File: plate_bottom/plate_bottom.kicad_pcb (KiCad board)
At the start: 2 copper layers, 180.2 x 118.1 mm, 0 parts

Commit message: Holes
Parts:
- added HM1: CaseHole, used_footprints:Hole_Mount_M4, F.Cu at (215.4, 123.7)
- added HM10: CaseHole, used_footprints:Hole_Mount_M4, F.Cu at (190.8, 74.8)
- added HM11: CaseHole, used_footprints:Hole_Mount_M4, F.Cu at (152.7, 68.5)
- added HM12: CaseHole, used_footprints:Hole_Mount_M4, F.Cu at (220.1, 69.2)
- added HM2: CaseHole, used_footprints:Hole_Mount_M4, F.Cu at (191.3, 55.2)
- added HM3: CaseHole, used_footprints:Hole_Mount_M4, F.Cu at (240.8, 109.5)
- added HM4: CaseHole, used_footprints:Hole_Mount_M4, F.Cu at (164.4, 116.7)
- added HM5: CaseHole, used_footprints:Hole_Mount_M4, F.Cu at (95.5, 98.6)
- added HM6: CaseHole, used_footprints:Hole_Mount_M4, F.Cu at (114.6, 98.7)
- added HM7: CaseHole, used_footprints:Hole_Mount_M4, F.Cu at (114.5, 59.9)
- added HM8: CaseHole, used_footprints:Hole_Mount_M4, F.Cu at (114.5, 79.7)
- added HM9: CaseHole, used_footprints:Hole_Mount_M4, F.Cu at (152.7, 53.4)
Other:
- outline, holes or cut-outs redrawn
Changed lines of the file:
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@@
     (tracks 0)
     (zones 0)
-    (modules 0)
+    (modules 12)
     (nets 1)
   )
@@
     (uvia_drill 0.1)
   )
+  (module used_footprints:Hole_Mount_M4 (layer F.Cu)
+    (at 215.4 123.65 36)
+    (fp_text reference HM1 (at -0.01 -2.09 36) (layer F.SilkS) hide
+      (effects (font (size 1 1) (thickness 0.15)))
+    )
+    (fp_text value CaseHole (at 0.5 -3.77 36) (layer F.Fab) hide
+      (effects (font (size 1 1) (thickness 0.15)))
+    )
+    (pad "" np_thru_hole circle (at -0.117557 0.161803 36) (size 2.2 2.2) (drill 2.2) (layers *.Cu *.Mask))
+  )
+  (module used_footprints:Hole_Mount_M4 (layer F.Cu)
+    (at 164.44712 116.70512)
+    (fp_text reference HM4 (at -0.01 -2.09) (layer Dwgs.User) hide
+      (effects (font (size 1 1) (thickness 0.15)))
+    )
+    (fp_text value CaseHole (at 0.5 -3.77) (layer F.Fab) hide
+      (effects (font (size 1 1) (thickness 0.15)))
+    )
+    (pad "" np_thru_hole circle (at 0.00288 -0.70512) (size 2.2 2.2) (drill 2.2) (layers *.Cu *.Mask))
+  )
+  (module used_footprints:Hole_Mount_M4 (layer F.Cu)
+    (at 114.55 59.9)
+    (fp_text reference HM7 (at -0.01 -2.09) (layer F.SilkS) hide
+      (effects (font (size 1 1) (thickness 0.15)))
+    )
+    (fp_text value CaseHole (at 0.5 -3.77) (layer F.Fab) hide
+      (effects (font (size 1 1) (thickness 0.15)))
+    )
+    (pad "" np_thru_hole circle (at 0 0) (size 2.2 2.2) (drill 2.2) (layers *.Cu *.Mask))
+  )
+  (module used_footprints:Hole_Mount_M4 (layer F.Cu)
+    (at 152.65 53.35)
+    (fp_text reference HM9 (at -0.01 -2.09) (layer F.SilkS) hide
+      (effects (font (size 1 1) (thickness 0.15)))
+    )
+    (fp_text value CaseHole (at 0.5 -3.77) (layer F.Fab) hide
+      (effects (font (size 1 1) (thickness 0.15)))
+    )
+    (pad "" np_thru_hole circle (at -0.65 -0.5) (size 2.2 2.2) (drill 2.2) (layers *.Cu *.Mask))
+  )
+  (module used_footprints:Hole_Mount_M4 (layer F.Cu)
+    (at 190.75 74.85)
+    (fp_text reference HM10 (at -0.01 -2.09) (layer F.SilkS) hide
+      (effects (font (size 1 1) (thickness 0.15)))
+    )
+    (fp_text value CaseHole (at 0.5 -3.77) (layer F.Fab) hide
+      (effects (font (size 1 1) (thickness 0.15)))
+    )
+    (pad "" np_thru_hole circle (at 0 0) (size 2.2 2.2) (drill 2.2) (layers *.Cu *.Mask))
+  )
+  (module used_footprints:Hole_Mount_M4 (layer F.Cu)
+    (at 95.5 98.56832)
+    (fp_text reference HM5 (at -0.01 -2.09) (layer Dwgs.User) hide
+      (effects (font (size 1 1) (thickness 0.15)))
+    )
+    (fp_text value CaseHole (at 0.5 -3.77) (layer F.Fab) hide
+      (effects (font (size 1 1) (thickness 0.15)))
+    )
+    (pad "" np_thru_hole circle (at 0 0.08168) (size 2.2 2.2) (drill 2.2) (layers *.Cu *.Mask))
+  )
+  (module used_footprints:Hole_Mount_M4 (layer F.Cu)
+    (at 191.2725 55.183451 14.5)
+    (fp_text reference HM2 (at -0.01 -2.09 14.5) (layer Dwgs.User) hide
+      (effects (font (size 1 1) (thickness 0.15)))
+    )
+    (fp_text value CaseHole (at 0.5 -3.77 14.5) (layer F.Fab) hide
+      (effects (font (size 1 1) (thickness 0.15)))
+    )
+    (pad "" np_thru_hole circle (at 0.035 -0.0255 14.5) (size 2.2 2.2) (drill 2.2) (layers *.Cu *.Mask))
+  )
+  (module used_footprints:Hole_Mount_M4 (layer F.Cu)
+    (at 152.7 68.55)
+    (fp_text reference HM11 (at -0.01 -2.09) (layer F.SilkS) hide
+      (effects (font (size 1 1) (thickness 0.15)))
+    )
+    (fp_text value CaseHole (at 0.5 -3.77) (layer F.Fab) hide
+      (effects (font (size 1 1) (thickness 0.15)))
+    )
+    (pad "" np_thru_hole circle (at 0 0) (size 2.2 2.2) (drill 2.2) (layers *.Cu *.Mask))
+  )
+  (module used_footprints:Hole_Mount_M4 (layer F.Cu)
+    (at 114.6 98.7)
+    (fp_text reference HM6 (at -0.01 -2.09) (layer Dwgs.User) hide
+      (effects (font (size 1 1) (thickness 0.15)))
+    )
+    (fp_text value CaseHole (at 0.5 -3.77) (layer F.Fab) hide
+      (effects (font (size 1 1) (thickness 0.15)))
+    )
+    (pad "" np_thru_hole circle (at -0.05 -0.1) (size 2.2 2.2) (drill 2.2) (layers *.Cu *.Mask))
+  )
+  (module used_footprints:Hole_Mount_M4 (layer F.Cu)
+    (at 114.55 79.65)
+    (fp_text reference HM8 (at -0.01 -2.09) (layer F.SilkS) hide
+      (effects (font (size 1 1) (thickness 0.15)))
+    )
+    (fp_text value CaseHole (at 0.5 -3.77) (layer F.Fab) hide
+      (effects (font (size 1 1) (thickness 0.15)))
+    )
+    (pad "" np_thru_hole circle (at 0 -0.1) (size 2.2 2.2) (drill 2.2) (layers *.Cu *.Mask))
+  )
+  (module used_footprints:Hole_Mount_M4 (layer F.Cu)
+    (at 240.85 109.5)
+    (fp_text reference HM3 (at -0.01 -2.09) (layer Dwgs.User) hide
+      (effects (font (size 1 1) (thickness 0.15)))
+    )
+    (fp_text value CaseHole (at 0.5 -3.77) (layer F.Fab) hide
+      (effects (font (size 1 1) (thickness 0.15)))
+    )
+    (pad "" np_thru_hole circle (at 0.005 -0.12) (size 2.2 2.2) (drill 2.2) (layers *.Cu *.Mask))
+  )
+  (module used_footprints:Hole_Mount_M4 (layer F.Cu)
+    (at 220.1 69.2)
+    (fp_text reference HM12 (at 0.1 -1.7) (layer F.SilkS) hide
+      (effects (font (size 1 1) (thickness 0.15)))
+    )
+    (fp_text value CaseHole (at 0.5 -3.77) (layer F.Fab) hide
+      (effects (font (size 1 1) (thickness 0.15)))
+    )
+    (pad "" np_thru_hole circle (at 0 0) (size 2.2 2.2) (drill 2.2) (layers *.Cu *.Mask))
+  )
+  (gr_line (start 254.5 101.65) (end 247.4 115.6) (layer Edge.Cuts) (width 0.05))
+  (gr_line (start 246.1 117.8) (end 247.4 115.6) (layer Edge.Cuts) (width 0.05))
+  (gr_line (start 255.2 99.65) (end 254.5 101.65) (layer Edge.Cuts) (width 0.05))
+  (gr_line (start 246.1 117.8) (end 233.991655 134.471139) (layer Edge.Cuts) (width 0.05))
+  (gr_line (start 256.75 89.9) (end 255.2 99.65) (layer Edge.Cuts) (width 0.05))
   (gr_line (start 256.75 89.9) (end 256.75 89.45) (layer Edge.Cuts) (width 0.05))
   (gr_line (start 251.215825 54.501067) (end 256.75 89.45) (layer Edge.Cuts) (width 0.05))
@@
   (gr_line (start 93.15 100.8) (end 77.55 100.8) (layer Edge.Cuts) (width 0.05))
   (gr_line (start 227.4 56.25) (end 209.65 56.25) (layer Edge.Cuts) (width 0.05))
-  (gr_line (start 256.75 89.9) (end 254.75 102.5) (layer Edge.Cuts) (width 0.05))
-  (gr_line (start 254.6 102.9) (end 249.3 113.3) (layer Edge.Cuts) (width 0.05))
-  (gr_line (start 248.9 113.95) (end 233.991655 134.471139) (layer Edge.Cuts) (width 0.05))
-  (gr_line (start 254.75 102.5) (end 254.6 102.9) (layer Edge.Cuts) (width 0.05))
-  (gr_line (start 248.9 113.95) (end 249.3 113.3) (layer Edge.Cuts) (width 0.05))
   (gr_line (start 248.927579 52.838559) (end 227.4 56.25) (layer Edge.Cuts) (width 0.05))
   (gr_line (start 191.7 55.25) (end 199 55.25) (layer Edge.Cuts) (width 0.05))

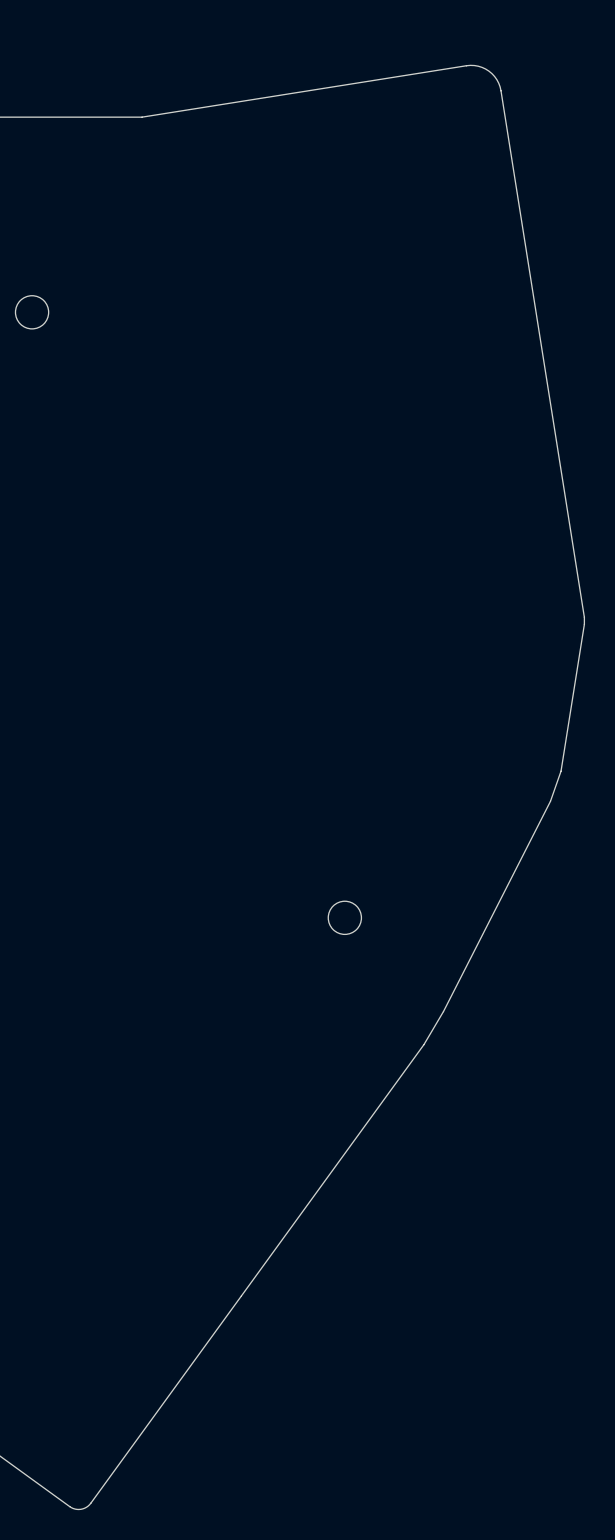
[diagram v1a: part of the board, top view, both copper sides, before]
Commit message: Edges cuts
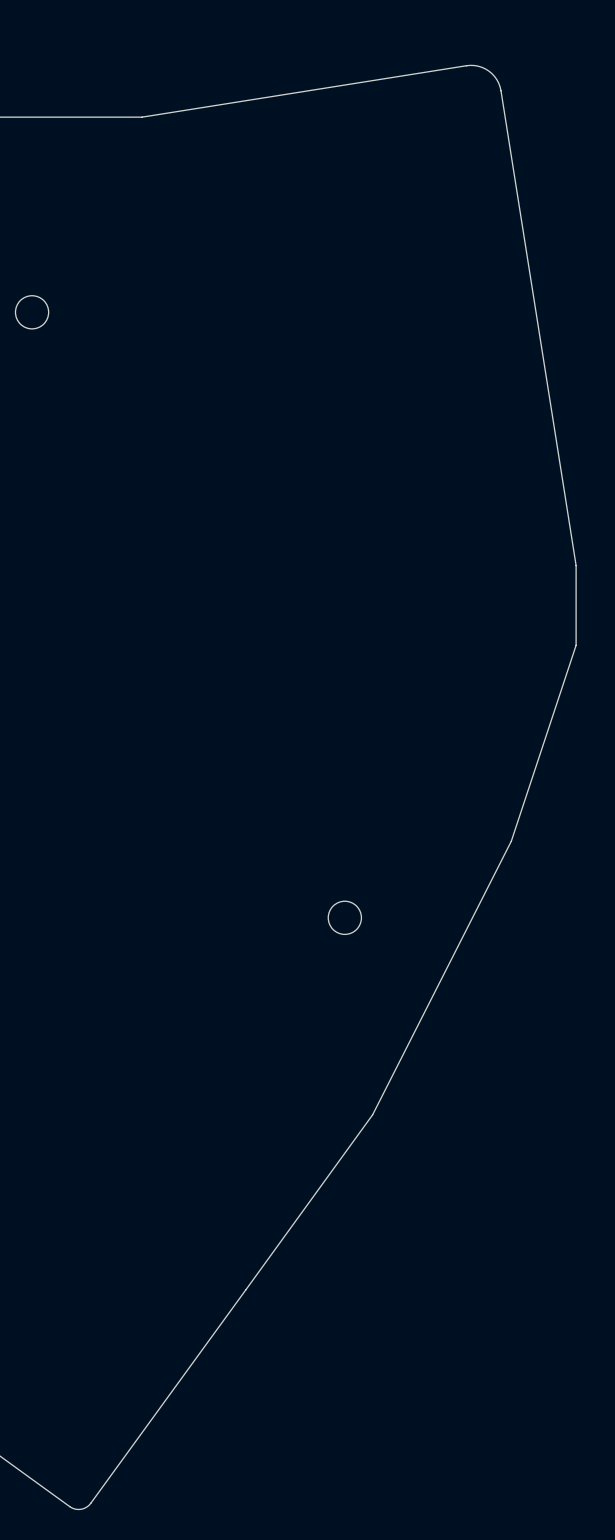
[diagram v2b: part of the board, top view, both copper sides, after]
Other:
- board size 180.2 x 118.1 mm -> 179.6 x 118.1 mm
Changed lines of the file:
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@@
   (general
     (thickness 1.6)
-    (drawings 119)
+    (drawings 117)
     (tracks 0)
     (zones 0)
@@
     (pad "" np_thru_hole circle (at 0 0) (size 2.2 2.2) (drill 2.2) (layers *.Cu *.Mask))
   )
-  (gr_line (start 254.5 101.65) (end 247.4 115.6) (layer Edge.Cuts) (width 0.05))
-  (gr_line (start 246.1 117.8) (end 247.4 115.6) (layer Edge.Cuts) (width 0.05))
-  (gr_line (start 255.2 99.65) (end 254.5 101.65) (layer Edge.Cuts) (width 0.05))
-  (gr_line (start 246.1 117.8) (end 233.991655 134.471139) (layer Edge.Cuts) (width 0.05))
-  (gr_line (start 256.75 89.9) (end 255.2 99.65) (layer Edge.Cuts) (width 0.05))
-  (gr_line (start 256.75 89.9) (end 256.75 89.45) (layer Edge.Cuts) (width 0.05))
-  (gr_line (start 251.215825 54.501067) (end 256.75 89.45) (layer Edge.Cuts) (width 0.05))
+  (gr_line (start 242.7 122.45) (end 234.283043 134.070973) (layer Edge.Cuts) (width 0.05))
+  (gr_line (start 256.2 86) (end 256.2 91.3) (layer Edge.Cuts) (width 0.05))
+  (gr_line (start 251.9 104.3) (end 242.7 122.45) (layer Edge.Cuts) (width 0.05))
+  (gr_line (start 234.283043 134.070973) (end 223.996802 148.22877) (layer Edge.Cuts) (width 0.05))
+  (gr_line (start 256.2 91.3) (end 251.9 104.3) (layer Edge.Cuts) (width 0.05))
+  (gr_line (start 251.215825 54.501067) (end 256.2 86) (layer Edge.Cuts) (width 0.05))
   (gr_line (start 96.6 117.55) (end 139.35 117.55) (layer Edge.Cuts) (width 0.05))
   (gr_arc (start 95.500338 98.622885) (end 93.15 100.8) (angle -48.97400321) (layer Edge.Cuts) (width 0.05))
@@
   (gr_line (start 207.9 137.8) (end 222.6 148.45) (layer Edge.Cuts) (width 0.05))
   (gr_arc (start 223.187786 147.640984) (end 222.6 148.45) (angle -90) (layer Edge.Cuts) (width 0.05))
-  (gr_line (start 223.996802 148.22877) (end 233.991655 134.471139) (layer Edge.Cuts) (width 0.05))
   (gr_line (start 189.55 131.85) (end 207.9 137.8) (layer Edge.Cuts) (width 0.05))
   (gr_arc (start 143.003464 134.39995) (end 142.015776 134.556384) (angle -90) (layer Edge.Cuts) (width 0.05))

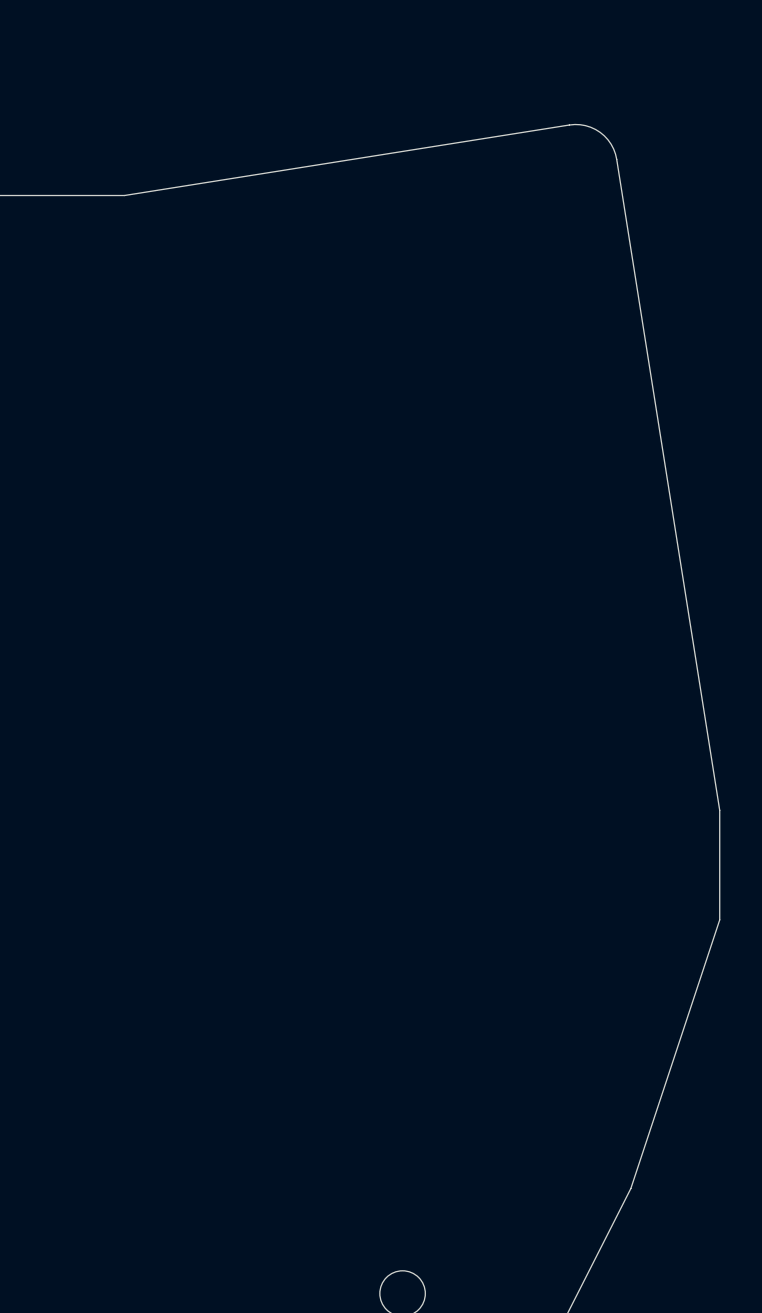
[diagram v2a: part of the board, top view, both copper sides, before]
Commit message: Added underglow LEDs and many more...
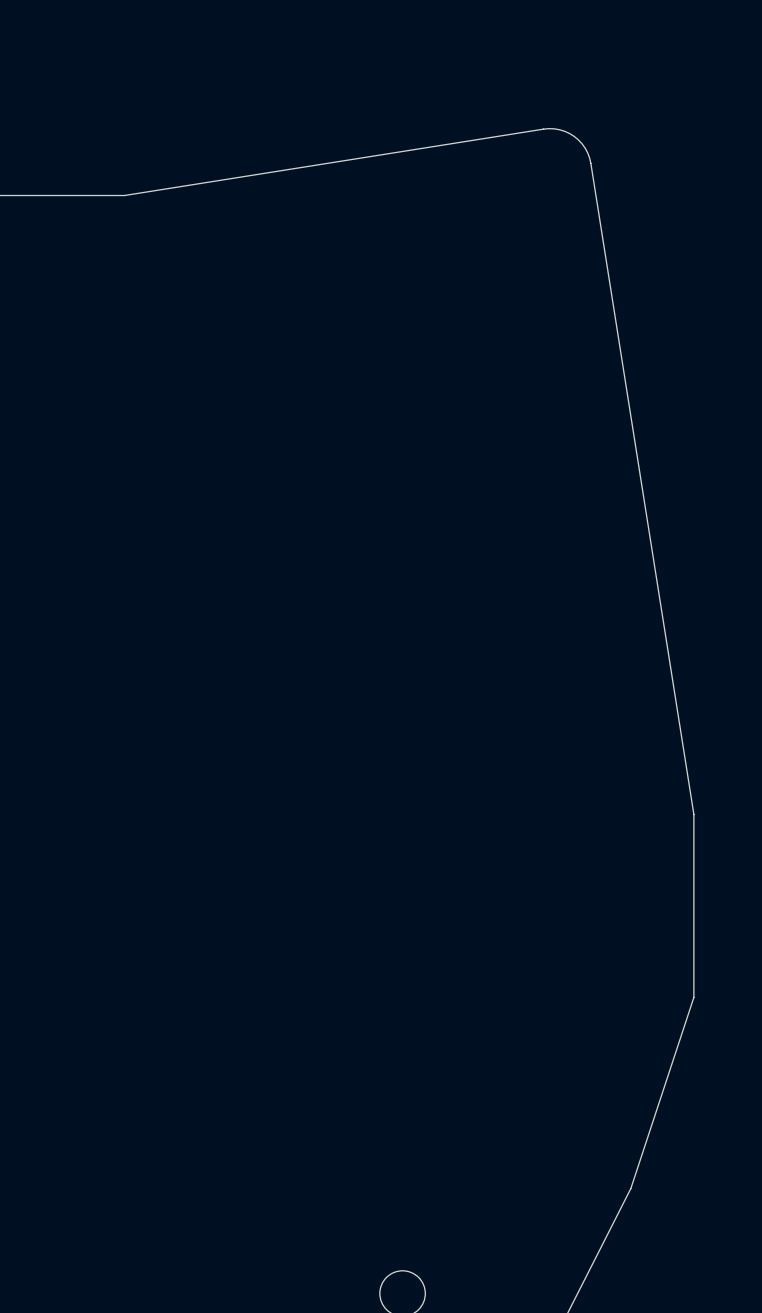
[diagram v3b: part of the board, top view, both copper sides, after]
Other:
- board size 179.6 x 118.1 mm -> 178.4 x 118.1 mm
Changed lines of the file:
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@@
     (pad "" np_thru_hole circle (at 0 0) (size 2.2 2.2) (drill 2.2) (layers *.Cu *.Mask))
   )
+  (gr_line (start 247.677579 53.038559) (end 227.4 56.25) (layer Edge.Cuts) (width 0.05))
+  (gr_line (start 249.965825 54.701067) (end 254.95 86.2) (layer Edge.Cuts) (width 0.05))
+  (gr_line (start 254.95 95.05) (end 251.9 104.3) (layer Edge.Cuts) (width 0.05))
+  (gr_line (start 251.9 104.3) (end 242.7 122.45) (layer Edge.Cuts) (width 0.05))
+  (gr_arc (start 247.990448 55.013936) (end 249.965825 54.701067) (angle -90) (layer Edge.Cuts) (width 0.05))
+  (gr_line (start 254.95 86.2) (end 254.95 95.05) (layer Edge.Cuts) (width 0.05))
   (gr_line (start 242.7 122.45) (end 234.283043 134.070973) (layer Edge.Cuts) (width 0.05))
-  (gr_line (start 256.2 86) (end 256.2 91.3) (layer Edge.Cuts) (width 0.05))
-  (gr_line (start 251.9 104.3) (end 242.7 122.45) (layer Edge.Cuts) (width 0.05))
   (gr_line (start 234.283043 134.070973) (end 223.996802 148.22877) (layer Edge.Cuts) (width 0.05))
-  (gr_line (start 256.2 91.3) (end 251.9 104.3) (layer Edge.Cuts) (width 0.05))
-  (gr_line (start 251.215825 54.501067) (end 256.2 86) (layer Edge.Cuts) (width 0.05))
   (gr_line (start 96.6 117.55) (end 139.35 117.55) (layer Edge.Cuts) (width 0.05))
   (gr_arc (start 95.500338 98.622885) (end 93.15 100.8) (angle -48.97400321) (layer Edge.Cuts) (width 0.05))
@@
   (gr_line (start 93.15 100.8) (end 77.55 100.8) (layer Edge.Cuts) (width 0.05))
   (gr_line (start 227.4 56.25) (end 209.65 56.25) (layer Edge.Cuts) (width 0.05))
-  (gr_line (start 248.927579 52.838559) (end 227.4 56.25) (layer Edge.Cuts) (width 0.05))
   (gr_line (start 191.7 55.25) (end 199 55.25) (layer Edge.Cuts) (width 0.05))
   (gr_arc (start 199 55.749998) (end 199 56.249996) (angle -180) (layer Edge.Cuts) (width 0.05))
-  (gr_arc (start 249.240448 54.813936) (end 251.215825 54.501067) (angle -90) (layer Edge.Cuts) (width 0.05))
   (gr_arc (start 203 55.749999) (end 203 55.25) (angle -180) (layer Edge.Cuts) (width 0.05))
 )
